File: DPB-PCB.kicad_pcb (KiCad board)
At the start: 2 copper layers, 2 parts, among them J1 USB-C, U1 ESP32-S3-WROOM-1-N4R2

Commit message: up
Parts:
- added C1: 10u 50V, Capacitor_SMD:C_1206_3216Metric, F.Cu at (93.8, 66.7)
- added C2: 100n 50V, Capacitor_SMD:C_01005_0402Metric, F.Cu at (109.2, 72.2)
- added C3: 22u 10V, Capacitor_SMD:C_1206_3216Metric, F.Cu at (93.8, 70.0)
- added C4: 22u 10V, Capacitor_SMD:C_1206_3216Metric, F.Cu at (93.8, 73.4)
- added C5: 10u 50V, Capacitor_SMD:C_1206_3216Metric, F.Cu at (93.8, 76.7)
- added C6: 10u 50V, Capacitor_SMD:C_1206_3216Metric, F.Cu at (93.8, 80.1)
- added C7: 2n2 50V, Capacitor_SMD:C_0805_2012Metric, F.Cu at (93.2, 83.2)
- added D2: SS54, Library:DO-214AC, F.Cu at (103.0, 79.9)
- added D3: BZV55B5V6, Diode_SMD:D_MiniMELF, F.Cu at (102.8, 83.1)
- added L1: 4u7, Library:IND_ASPI-0530LR-3R3M-T2, F.Cu at (103.8, 74.8)
- added Q1: MMBT5551L, Package_TO_SOT_SMD:SOT-23, F.Cu at (91.4, 54.3)
- added Q2: AO3401A, Package_TO_SOT_SMD:SOT-23, F.Cu at (108.9, 80.5)
- added R1: 3k3, Resistor_SMD:R_0402_1005Metric, F.Cu at (98.1, 66.0)
- added R2: 130k, Resistor_SMD:R_0402_1005Metric, F.Cu at (98.1, 68.0)
- added R3: 10k, Resistor_SMD:R_0402_1005Metric, F.Cu at (98.1, 70.0)
- added R4: 75k, Resistor_SMD:R_0402_1005Metric, F.Cu at (98.1, 72.0)
- added R5: 24k, Resistor_SMD:R_0402_1005Metric, F.Cu at (98.1, 73.9)
- added R6: 16k, Resistor_SMD:R_0805_2012Metric, F.Cu at (108.7, 84.2)
- added U2: CP2102N-Axx-xQFN28, Package_DFN_QFN:QFN-28-1EP_5x5mm_P0.5mm_EP3.35x3.35mm, F.Cu at (117.0, 79.1)
- added U3: USBLC6-4SC6, Library:SOT95P280X145-6N, F.Cu at (123.2, 77.8)
- added U4: RT7272BGSP, Library:SOIC127P599X175-9N, F.Cu at (104.4, 68.2)
- moved J1 1.36 mm to (82.0, 56.4), turned to 0 degrees

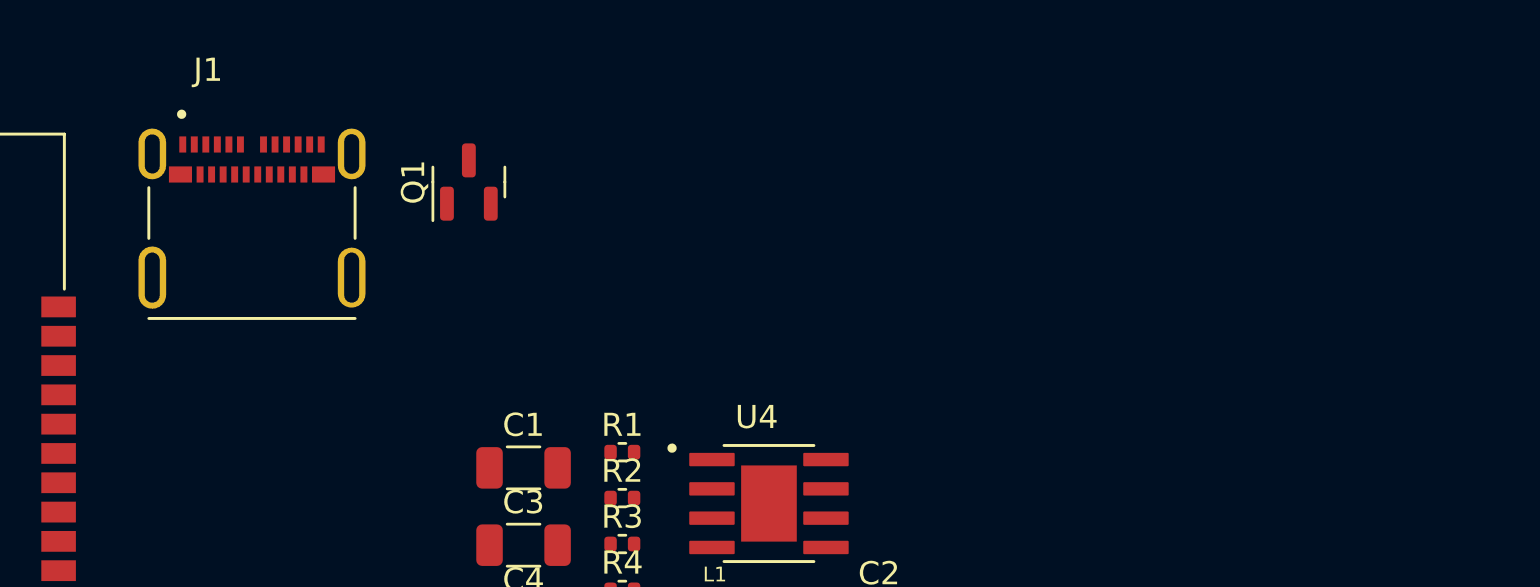
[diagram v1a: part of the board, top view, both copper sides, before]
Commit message: All components have been added
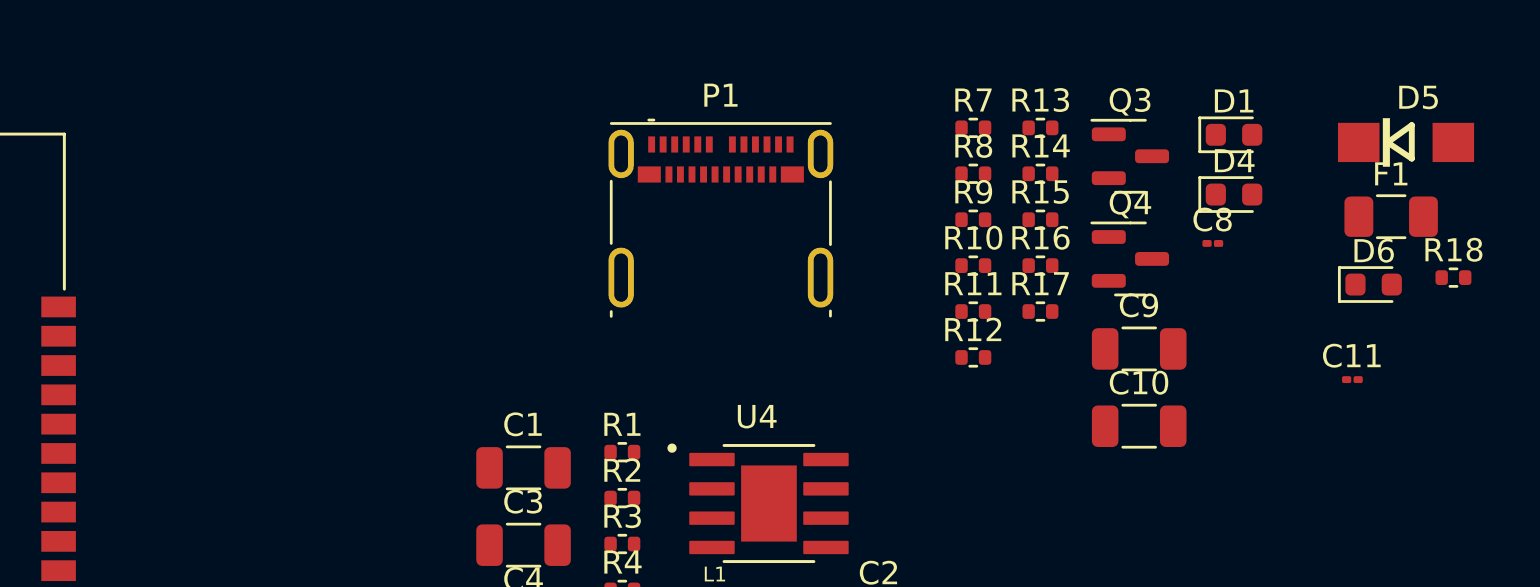
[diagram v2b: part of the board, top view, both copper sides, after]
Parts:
- removed J1: USB-C, Library:MOLEX_USB_TYPE_C
- removed Q1: MMBT5551L, Package_TO_SOT_SMD:SOT-23
- added C10: 10u 50V, Capacitor_SMD:C_1206_3216Metric, F.Cu at (120.5, 64.9)
- added C11: 100n 50V, Capacitor_SMD:C_01005_0402Metric, F.Cu at (129.7, 62.8)
- added C8: 100n 50V, Capacitor_SMD:C_01005_0402Metric, F.Cu at (123.7, 56.9)
- added C9: 10u 50V, Capacitor_SMD:C_1206_3216Metric, F.Cu at (120.5, 61.5)
- added D1: LED_YLW, LED_SMD:LED_0603_1608Metric, F.Cu at (124.6, 52.2)
- added D4: LED_BLUE, LED_SMD:LED_0603_1608Metric, F.Cu at (124.6, 54.8)
- added D5: SS54, Library:DO-214AC, F.Cu at (132.1, 52.6)
- added D6: LED_GREEN, LED_SMD:LED_0603_1608Metric, F.Cu at (130.7, 58.7)
- added F1: 60V 120mA, Fuse:Fuse_1206_3216Metric, F.Cu at (131.4, 55.8)
- added P1: USB_C_Prog, Connector_USB:USB_C_Receptacle_Molex_105450-0101, F.Cu at (102.4, 55.9)
- added Q3: MMBT5551, Package_TO_SOT_SMD:SOT-23, F.Cu at (120.1, 53.2)
- added Q4: MMBT5551, Package_TO_SOT_SMD:SOT-23, F.Cu at (120.1, 57.6)
- added R10: 1k, Resistor_SMD:R_0402_1005Metric, F.Cu at (113.3, 57.9)
- added R11: 1k, Resistor_SMD:R_0402_1005Metric, F.Cu at (113.3, 59.9)
- added R12: 10k, Resistor_SMD:R_0402_1005Metric, F.Cu at (113.3, 61.9)
- added R13: 10k, Resistor_SMD:R_0402_1005Metric, F.Cu at (116.2, 51.9)
- added R14: 0, Resistor_SMD:R_0402_1005Metric, F.Cu at (116.2, 53.9)
- added R15: 0, Resistor_SMD:R_0402_1005Metric, F.Cu at (116.2, 55.9)
- added R16: 56k, Resistor_SMD:R_0402_1005Metric, F.Cu at (116.2, 57.9)
- added R17: 120k, Resistor_SMD:R_0402_1005Metric, F.Cu at (116.2, 59.9)
- added R18: 1k, Resistor_SMD:R_0402_1005Metric, F.Cu at (134.1, 58.4)
- added R7: 5k1, Resistor_SMD:R_0402_1005Metric, F.Cu at (113.3, 51.9)
- added R8: 5k1, Resistor_SMD:R_0402_1005Metric, F.Cu at (113.3, 53.9)
- added R9: 1k, Resistor_SMD:R_0402_1005Metric, F.Cu at (113.3, 55.9)
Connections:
- D2 pad A: +VDC -> Net-(D2-PadA)
- U1 pad 1: Net-(U1-GND-Pad1) -> GND
- U1 pad 2: unconnected-(U1-3V3-Pad2) -> +3.3V
- U1 pad 27: unconnected-(U1-IO0-Pad27) -> GPIO0
- U1 pad 3: unconnected-(U1-EN-Pad3) -> CHIP_PU
- U1 pad 36: unconnected-(U1-RXD0-Pad36) -> MCU_RX
- U1 pad 37: unconnected-(U1-TXD0-Pad37) -> MCU_TX
- U1 pad 40: Net-(U1-GND-Pad1) -> GND
- U1 pad 41_1: Net-(U1-GND-Pad1) -> GND
- U1 pad 41_2: Net-(U1-GND-Pad1) -> GND
- U1 pad 41_3: Net-(U1-GND-Pad1) -> GND
- U1 pad 41_4: Net-(U1-GND-Pad1) -> GND
- U1 pad 41_5: Net-(U1-GND-Pad1) -> GND
- U1 pad 41_6: Net-(U1-GND-Pad1) -> GND
- U1 pad 41_7: Net-(U1-GND-Pad1) -> GND
- U1 pad 41_8: Net-(U1-GND-Pad1) -> GND
- U1 pad 41_9: Net-(U1-GND-Pad1) -> GND
- U2 pad 18: unconnected-(U2-~{RXT}/GPIO.1-Pad18) -> /USB/RXT
- U2 pad 19: unconnected-(U2-~{TXT}/GPIO.0-Pad19) -> /USB/TXT
- U2 pad 24: unconnected-(U2-~{RTS}-Pad24) -> /USB/RTS
- U2 pad 25: unconnected-(U2-RXD-Pad25) -> MCU_TX
- U2 pad 26: unconnected-(U2-TXD-Pad26) -> MCU_RX
- U2 pad 28: unconnected-(U2-~{DTR}-Pad28) -> /USB/DTR
- U2 pad 29: Net-(U2-GND-Pad29) -> GND
- U2 pad 3: Net-(U2-GND-Pad29) -> GND
- U2 pad 4: unconnected-(U2-D+-Pad4) -> /USB/COM_D+
- U2 pad 5: unconnected-(U2-D--Pad5) -> /USB/COM_D-
- U2 pad 6: unconnected-(U2-VDD-Pad6) -> +3.3V
- U2 pad 7: unconnected-(U2-VREGIN-Pad7) -> +3.3V
- U2 pad 8: unconnected-(U2-VBUS-Pad8) -> Net-(U2-VBUS)
- U2 pad 9: unconnected-(U2-~{RST}-Pad9) -> Net-(U2-~{RST})
- U3 pad 1: unconnected-(U3-IO1-Pad1) -> /USB/COM_D+
- U3 pad 2: unconnected-(U3-GND-Pad2) -> GND
- U3 pad 3: unconnected-(U3-IO2-Pad3) -> /USB/COM_D-
- U3 pad 4: unconnected-(U3-IO3-Pad4) -> /USB/D-
- U3 pad 5: unconnected-(U3-VBUS-Pad5) -> VBUS
- U3 pad 6: unconnected-(U3-IO4-Pad6) -> /USB/D+

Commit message: Divided project
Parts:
- removed U3: USBLC6-4SC6, Library:SOT95P280X145-6N
- added 3V3: ~, TestPoint:TestPoint_Pad_D2.0mm, F.Cu at (43.8, 90.3)
- added C12: 10u 50V, Capacitor_SMD:C_1206_3216Metric, F.Cu at (37.9, 136.8)
- added C13: 100n 50V, Capacitor_SMD:C_01005_0402Metric, F.Cu at (57.0, 134.1)
- added C14: 100n 50V, Capacitor_SMD:C_01005_0402Metric, F.Cu at (57.0, 135.8)
- added CS1: ~, TestPoint:TestPoint_Pad_D2.0mm, F.Cu at (43.8, 94.4)
- added D7: LED_GREEN, LED_SMD:LED_0603_1608Metric, F.Cu at (42.8, 136.4)
- added D8: LED_YELLOW, LED_SMD:LED_0603_1608Metric, F.Cu at (60.2, 134.6)
- added D9: SMF05CT1G, Package_TO_SOT_SMD:SOT-23-6, F.Cu at (40.3, 118.8)
- added GND1: ~, TestPoint:TestPoint_Pad_D2.0mm, F.Cu at (43.8, 98.4)
- added H3: M3, MountingHole:MountingHole_3.2mm_M3_Pad_TopBottom, F.Cu at (54.9, 91.2)
- added H4: M3, MountingHole:MountingHole_3.2mm_M3_Pad_TopBottom, F.Cu at (54.9, 99.1)
- added H5: M3, MountingHole:MountingHole_3.2mm_M3_Pad_TopBottom, F.Cu at (54.9, 107.1)
- added H6: M3, MountingHole:MountingHole_3.2mm_M3_Pad_TopBottom, F.Cu at (54.9, 115.0)
- added INT1: ~, TestPoint:TestPoint_Pad_D2.0mm, F.Cu at (43.8, 102.5)
- added J1: LCD_Conn, Connector_PinHeader_2.54mm:PinHeader_1x14_P2.54mm_Vertical, F.Cu at (16.3, 89.5)
- added J2: XT60 - M, Library:XT60-SURF, F.Cu at (27.6, 103.2)
- added J3: IMU_FFC_Conn, Connector_FFC-FPC:Hirose_FH12-8S-0.5SH_1x08-1MP_P0.50mm_Horizontal, F.Cu at (43.3, 111.2)
- added J4: JTAG_Conn, Connector_PinHeader_2.54mm:PinHeader_1x06_P2.54mm_Vertical, F.Cu at (39.0, 89.9)
- added J5: IR_LED, Connector_JST:JST_EH_S2B-EH_1x02_P2.50mm_Horizontal, F.Cu at (22.2, 115.4)
- added J6: IR_SENSOR, Connector_JST:JST_EH_S2B-EH_1x02_P2.50mm_Horizontal, F.Cu at (31.7, 115.4)
- added MISO1: ~, TestPoint:TestPoint_Pad_D2.0mm, F.Cu at (47.9, 90.3)
- added MOSI1: ~, TestPoint:TestPoint_Pad_D2.0mm, F.Cu at (47.9, 94.4)
- added R19: 1k, Resistor_SMD:R_0402_1005Metric, F.Cu at (46.3, 136.1)
- added R20: 680, Resistor_SMD:R_0402_1005Metric, F.Cu at (46.3, 138.1)
- added R21: 10k, Resistor_SMD:R_0402_1005Metric, F.Cu at (59.6, 127.9)
- added R22: 1k, Resistor_SMD:R_0402_1005Metric, F.Cu at (59.6, 129.8)
- added R23: 1k, Resistor_SMD:R_0402_1005Metric, F.Cu at (59.6, 131.8)
- added R24: 100, Resistor_SMD:R_0603_1608Metric, F.Cu at (60.1, 137.2)
- added RV1: 10k, Potentiometer_SMD:Potentiometer_Bourns_TC33X_Vertical, F.Cu at (52.9, 135.7)
- added SCK1: ~, TestPoint:TestPoint_Pad_D2.0mm, F.Cu at (47.9, 98.4)
- added U5: AMS1117-3.3, Package_TO_SOT_SMD:SOT-223-3_TabPin2, F.Cu at (40.0, 131.0)
- added U7: LM358, Package_SO:SOIC-8_3.9x4.9mm_P1.27mm, F.Cu at (54.0, 130.1)
- added U9: USBLC6-4SC6, Package_TO_SOT_SMD:SOT-23-6, F.Cu at (52.3, 142.6)
- D6: value LED_GREEN -> LED_BLUE
- L1: value 4u7 -> 6u8; footprint Library:IND_ASPI-0530LR-3R3M-T2 -> Inductor_SMD:L_Chilisin_BMRx00060630
- R4: value 75k -> 33k
- R5: value 24k -> 5k6
- R6: value 16k -> 24k; footprint Resistor_SMD:R_0805_2012Metric -> Resistor_SMD:R_0402_1005Metric
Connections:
- net CHIP_PU renamed /EN
- net GPIO0 renamed /BOOT
- net MCU_RX renamed /RXD0
- net MCU_TX renamed /TXD0
- C3 pad 1: +3.3V -> +5V
- C4 pad 1: +3.3V -> +5V
- L1 pad 2: +3.3V -> +5V
- R4 pad 1: +3.3V -> +5V
- R5 pad 2: GND -> Net-(R20-Pad1)
- U1 pad 10: unconnected-(U1-IO17-Pad10) -> LCD_T_CS
- U1 pad 11: unconnected-(U1-IO18-Pad11) -> LCD_T_DOUT
- U1 pad 18: unconnected-(U1-IO10-Pad18) -> IMU_CS
- U1 pad 19: unconnected-(U1-IO11-Pad19) -> IMU_MOSI
- U1 pad 20: unconnected-(U1-IO12-Pad20) -> IMU_SCK
- U1 pad 21: unconnected-(U1-IO13-Pad21) -> IMU_MISO
- U1 pad 22: unconnected-(U1-IO14-Pad22) -> IMU_INT
- U1 pad 23: unconnected-(U1-IO21-Pad23) -> IR_INTERRUPT
- U1 pad 32: unconnected-(U1-IO39-Pad32) -> JTAG_TCK
- U1 pad 33: unconnected-(U1-IO40-Pad33) -> JTAG_TDO
- U1 pad 34: unconnected-(U1-IO41-Pad34) -> JTAG_TDI
- U1 pad 35: unconnected-(U1-IO42-Pad35) -> JTAG_TMS
- U1 pad 4: unconnected-(U1-IO4-Pad4) -> ESC_CMD
- U1 pad 5: unconnected-(U1-IO5-Pad5) -> LCD_CS
- U1 pad 6: unconnected-(U1-IO6-Pad6) -> LCD_RESET
- U1 pad 7: unconnected-(U1-IO7-Pad7) -> LCD_DC
- U1 pad 8: unconnected-(U1-IO15-Pad8) -> LCD_MOSI
- U1 pad 9: unconnected-(U1-IO16-Pad9) -> LCD_SCK

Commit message: DPB mainboard_v1 completed
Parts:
- removed the C10 at (120.5, 64.9)
- removed the J4 at (39.0, 89.9)
- removed P1: USB_C_Prog, Connector_USB:USB_C_Receptacle_Molex_105450-0101
- added C11: 10u 6V3, Capacitor_SMD:C_0402_1005Metric, F.Cu at (173.4, 117.2)
- added C12: 100n 50V, Capacitor_SMD:C_01005_0402Metric, F.Cu at (162.9, 118.5)
- added C15: 100n 50V, Capacitor_SMD:C_01005_0402Metric, F.Cu at (112.7, 93.4)
- added C2: 100n 50V, Capacitor_SMD:C_01005_0402Metric, F.Cu at (159.8, 94.9)
- added D6: 1N5819WS, Diode_SMD:D_SOD-323, F.Cu at (112.9, 101.2)
- added J1: USB_C_Prog, Connector_USB:USB_C_Receptacle_G-Switch_GT-USB-7010ASV, F.Cu at (170.3, 126.2)
- added J5: ESC_Conn, TerminalBlock:TerminalBlock_bornier-4_P5.08mm, F.Cu at (110.5, 82.6)
- added J8: USB_C_OTG, Connector_USB:USB_C_Receptacle_G-Switch_GT-USB-7010ASV, F.Cu at (104.5, 98.0)
- added R1: 47, Resistor_SMD:R_0402_1005Metric, F.Cu at (173.9, 87.8)
- added R11: 10k, Resistor_SMD:R_0402_1005Metric, F.Cu at (139.6, 119.3)
- added R12: 1k, Resistor_SMD:R_0402_1005Metric, F.Cu at (158.8, 94.6)
- added R2: 100, Resistor_SMD:R_0402_1005Metric, F.Cu at (172.6, 87.8)
- added R3: 100, Resistor_SMD:R_0402_1005Metric, F.Cu at (171.3, 87.8)
- added R32: 5k1, Resistor_SMD:R_0402_1005Metric, F.Cu at (110.4, 93.2)
- added R33: 5k1, Resistor_SMD:R_0402_1005Metric, F.Cu at (110.4, 102.9)
- added R38: 10, Resistor_SMD:R_0402_1005Metric, F.Cu at (173.9, 109.3)
- added R39: 10, Resistor_SMD:R_0402_1005Metric, F.Cu at (175.1, 109.3)
- added R4: 47, Resistor_SMD:R_0402_1005Metric, F.Cu at (158.9, 96.6)
- added R5: 47, Resistor_SMD:R_0402_1005Metric, F.Cu at (158.9, 99.2)
- added R6: 47, Resistor_SMD:R_0402_1005Metric, F.Cu at (170.1, 87.8)
- added R7: 47, Resistor_SMD:R_0402_1005Metric, F.Cu at (168.8, 87.8)
- added R8: 47, Resistor_SMD:R_0402_1005Metric, F.Cu at (166.2, 87.8)
- added R9: 47, Resistor_SMD:R_0402_1005Metric, F.Cu at (158.9, 103.5)
- added U6: USBLC6-4SC6, Package_TO_SOT_SMD:SOT-23-6, F.Cu at (112.9, 95.8)
- C14: renamed from C9; value 10u 50V -> 10u 6V3; footprint Capacitor_SMD:C_1206_3216Metric -> Capacitor_SMD:C_01005_0402Metric
- D5: value SS54 -> 1N5819WS; footprint Library:DO-214AC -> Diode_SMD:D_SOD-323
- J7: renamed from J2; footprint Library:XT60-SURF -> Connector_AMASS:AMASS_XT60PW-M_1x02_P7.20mm_Horizontal
- moved J2 160.6 mm to (176.7, 80.6), turned to -90 degrees
- moved H3 129.2 mm to (183.0, 82.0)
- moved J7 129.1 mm to (154.7, 125.4), turned to 180 degrees
- moved D9 120.7 mm to (157.7, 90.8), turned to -90 degrees
- moved U4 114.3 mm to (164.5, 120.4), turned to 135 degrees
- moved U1 113.8 mm to (173.7, 98.6), turned to -90 degrees
- moved H2 111.5 mm to (163.1, 134.0)
- moved C17 107.2 mm to (158.9, 102.6), turned to 180 degrees
- moved D1 106.1 mm to (147.5, 119.4), turned to 180 degrees
- moved R37 103.7 mm to (158.9, 101.7)
- moved R10 100.5 mm to (145.4, 119.3), turned to 90 degrees
- moved 3V1 99.3 mm to (143.1, 91.2)
- moved J3 96.4 mm to (135.8, 83.7), turned to 180 degrees
- moved J6 95.7 mm to (117.5, 123.8), turned to 135 degrees
- moved U3 95.1 mm to (134.5, 120.3)
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- renumbered 3V3 to 3V1, C11 to C1, C12 to C10, C8 to C13, C13 to C16, C14 to C17, C5 to C3, C6 to C4, C7 to C5, C1 to C6, C2 to C7, C3 to C8, C4 to C9, D7 to D1, D8 to D10, D6 to D3, D3 to D4, D4 to D7, D1 to D8, H3 to H1, H5 to H2, H4 to H3, H6 to H4, J1 to J2, J6 to J4, J5 to J6, Q2 to Q1, Q3 to Q2, Q4 to Q3, R19 to R10, R1 to R13, R18 to R14, R4 to R15, R5 to R16, R20 to R17, R6 to R18, R3 to R19, R2 to R20, R12 to R21, R13 to R22, R14 to R23, R15 to R24, R7 to R25, R8 to R26, R16 to R27, R17 to R28, R9 to R29, R10 to R30, R11 to R31, R24 to R34, R21 to R35, R22 to R36, R23 to R37, U4 to U2, U5 to U3, U9 to U4, U2 to U5
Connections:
- D9 pad 3: JTAG_TDO -> unconnected-(D9-K-Pad3)
- D9 pad 4: JTAG_TDI -> unconnected-(D9-K-Pad4)
- D9 pad 5: JTAG_TCK -> unconnected-(D9-K-Pad5)
- D9 pad 6: JTAG_TMS -> unconnected-(D9-K-Pad6)
- J2 pad 13: LCD_T_DOUT -> LCD_MISO
- J2 pad 9: unconnected-(J1-Pin_9-Pad9) -> LCD_MISO
- U1 pad 10: LCD_T_CS -> LCD_MISO
- U1 pad 11: LCD_T_DOUT -> /GPIO18
- U1 pad 13: unconnected-(U1-IO19-Pad13) -> USB_D-
- U1 pad 14: unconnected-(U1-IO20-Pad14) -> USB_D+
- U1 pad 18: IMU_CS -> V_ADC2
- U1 pad 19: IMU_MOSI -> /GPIO11
- U1 pad 20: IMU_SCK -> IMU_MISO
- U1 pad 21: IMU_MISO -> /GPIO13
- U1 pad 24: unconnected-(U1-IO47-Pad24) -> /GPIO47
- U1 pad 32: JTAG_TCK -> unconnected-(U1-IO39-Pad32)
- U1 pad 33: JTAG_TDO -> unconnected-(U1-IO40-Pad33)
- U1 pad 34: JTAG_TDI -> unconnected-(U1-IO41-Pad34)
- U1 pad 35: JTAG_TMS -> unconnected-(U1-IO42-Pad35)
- U1 pad 5: LCD_CS -> /GPIO5
- U1 pad 6: LCD_RESET -> /GPIO6
- U1 pad 7: LCD_DC -> /GPIO7
- U1 pad 8: LCD_MOSI -> /GPIO15
- U1 pad 9: LCD_SCK -> /GPIO16
- U4 pad 1: /USB/COM_D+ -> /USB/D+
- U4 pad 3: /USB/D+ -> /USB/D-
- U4 pad 4: /USB/COM_D- -> unconnected-(U4-I/O3-Pad4)
- U4 pad 6: /USB/D- -> unconnected-(U4-I/O4-Pad6)
- U5 pad 25: /TXD0 -> /USB/RXD
- U5 pad 26: /RXD0 -> /USB/TXD
- U5 pad 4: /USB/COM_D+ -> /USB/D+
- U5 pad 5: /USB/COM_D- -> /USB/D-
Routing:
- net +5V: track 0.00 -> 156.6 mm, vias 0 -> 7
- net USB_D+: track 0.00 -> 69.1 mm
- net USB_D-: track 0.00 -> 69.1 mm
- net ESC_CMD: track 0.00 -> 66.8 mm, vias 0 -> 2
- net +3.3V: track 0.00 -> 60.5 mm, vias 0 -> 22
- net Net-(R36-Pad2): track 0.00 -> 49.2 mm, vias 0 -> 2
- net IMU_CS: track 0.00 -> 45.1 mm, vias 0 -> 3
- net IMU_INT: track 0.00 -> 43.4 mm, vias 0 -> 3
- net IMU_SCK: track 0.00 -> 36.7 mm, vias 0 -> 3
- net IMU_MISO: track 0.00 -> 36.0 mm, vias 0 -> 3
- net V_ADC2: track 0.00 -> 34.7 mm
- net Net-(Q2-C): track 0.00 -> 33.8 mm, vias 0 -> 2
- net IMU_MOSI: track 0.00 -> 29.1 mm, vias 0 -> 3
- net LCD_MISO: track 0.00 -> 27.7 mm
- net LCD_MOSI: track 0.00 -> 27.3 mm
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- added copper zone on B.Cu, net +3.3V
- added copper zone on F.Cu, net +3.3V
- added copper zone on In2.Cu, net +3.3V
- added copper zone on B.Cu, net +5V
- added copper zone on F.Cu, net +5V
- added copper zone on F.Cu, net /Power Supply/SW
- added copper zone on B.Cu, net GND
- added copper zone on F.Cu, net GND
- added copper zone on In1.Cu, net GND
- added copper zone on F.Cu, net Net-(D2-PadA)
- added copper zone on F.Cu, net Net-(Q1-D)
- added copper zone on In2.Cu, net VBUS
- added copper zone on F.Cu, net VCC
- added copper zone on In2.Cu, net VCC
- added copper zone on In2.Cu, net V_USB
- added copper zone on B.Cu, net unconnected-(J1-SHIELD-PadS1)
- added copper zone on F.Cu, net unconnected-(J1-SHIELD-PadS1)
- added copper zone on In1.Cu, net unconnected-(J1-SHIELD-PadS1)
- added copper zone on In2.Cu, net unconnected-(J1-SHIELD-PadS1)
- added copper zone on B.Cu, net unconnected-(J8-SHIELD-PadS1)
- added copper zone on F.Cu, net unconnected-(J8-SHIELD-PadS1)
- added copper zone on In1.Cu, net unconnected-(J8-SHIELD-PadS1)
- added copper zone on In2.Cu, net unconnected-(J8-SHIELD-PadS1)
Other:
- board outline added: 86.6 x 60 mm
- copper layers 2 -> 4
- rule pad_to_mask_clearance: 0 -> 0.05
- board text added: "+"
- board text added: "0-36V"
- board text added: "3V3"
- board text added: "5V"
- board text added: "Active voltages"
- board text added: "BJT"
- board text added: "CS"
- board text added: "DC"
- board text added: "ESC"
- board text added: "GND"
- board text added: "IMU"
- board text added: "INT"
- board text added: "IR DIODE"
- board text added: "IR LED"
- board text added: "IR Sensitivity"
- board text added: "LED"
- board text added: "MISO"
- board text added: "MOSI"
- board text added: "NC"
- board text added: "OTG JTAG"
- board text added: "Obj"
- board text added: "PROG"
- board text added: "RST"
- board text added: "RX"
- board text added: "SCK"
- board text added: "SPI2"
- board text added: "TX"
- board text added: "T_CS"
- board text added: "T_MISO"
- board text added: "T_MOSI"
- board text added: "T_SCK"
- board text added: "VIN"
